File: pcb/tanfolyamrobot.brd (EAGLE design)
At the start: 81.3 x 58.7 mm, 79 parts, among them IC1 STM32F10XRXT6, IC2 7805, IC4 FT232RL, IC5 LD117AS33TR, M1 DRV8833, Q1 16MHz, Q2 BSS123, Q3 BSS123, Q4 BSS123, X2 PWR, X6 KUSBVX-BS1N

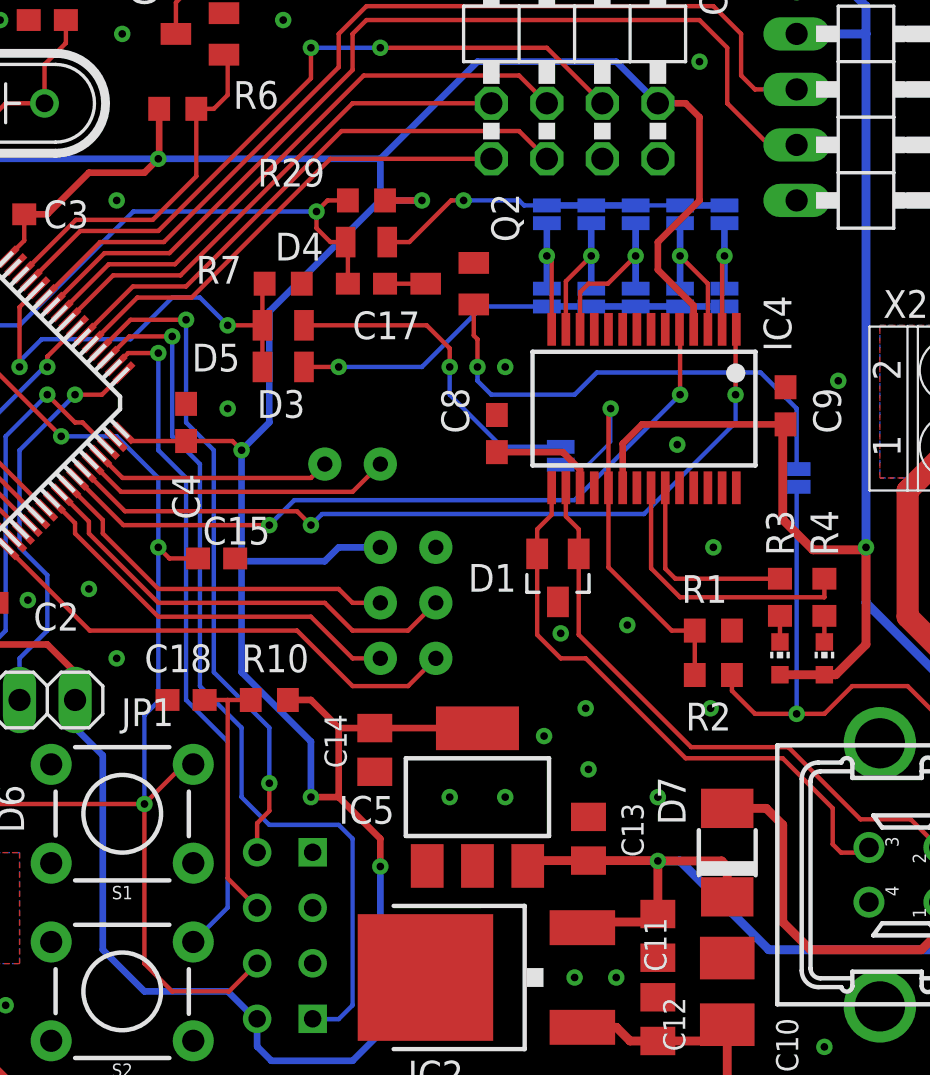
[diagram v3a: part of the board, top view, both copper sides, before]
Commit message: moved 5V_USB reset's cap to the gate of the mosfet (#1)
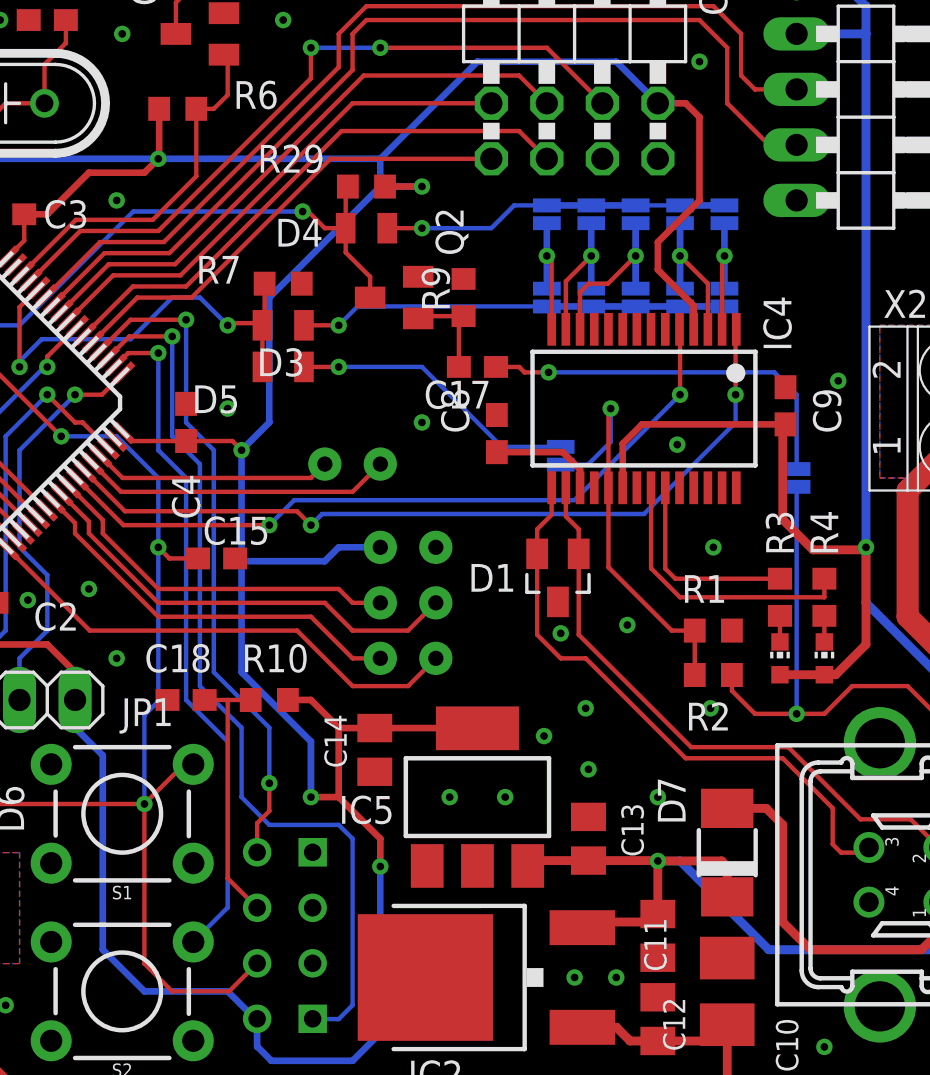
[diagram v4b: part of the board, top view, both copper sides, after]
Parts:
- added R9: 10K, rcl:R0603
- C17: value 22n -> 2u2
- moved C17 6.35 mm to (55.2, 34.9), turned to 180 degrees
- moved Q2 2.62 mm to (51.4, 38.1)
- moved D3 1.91 mm to (46.4, 36.8)
- moved D5 1.91 mm to (46.4, 34.9)
- moved D4 0.63 mm to (50.2, 41.3)
- moved R29 0.63 mm to (50.2, 43.2)
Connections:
- removed net N$6: JP14.2, Q2.1
- removed net N$9: C17.2, Q2.3
- new net N$2: C17.2, Q2.1, R9.1
- new net N$4: C17.1, JP14.2
- net GND: now also R9.2
- net RSTN: now also Q2.3; no longer C17.1
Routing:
- net N$6: track 22.3 -> 0.00 mm, vias 1 -> 0
- net N$4: track 0.00 -> 17.7 mm, vias 0 -> 1
- net N$2: track 0.00 -> 4.53 mm
- net N$8: track 15.3 -> 13.3 mm
- net N$9: track 1.86 -> 0.00 mm
- net RSTN: track 81.5 -> 83.3 mm
- net FTDI_BOOT0_OUT: track 20.4 -> 19.6 mm

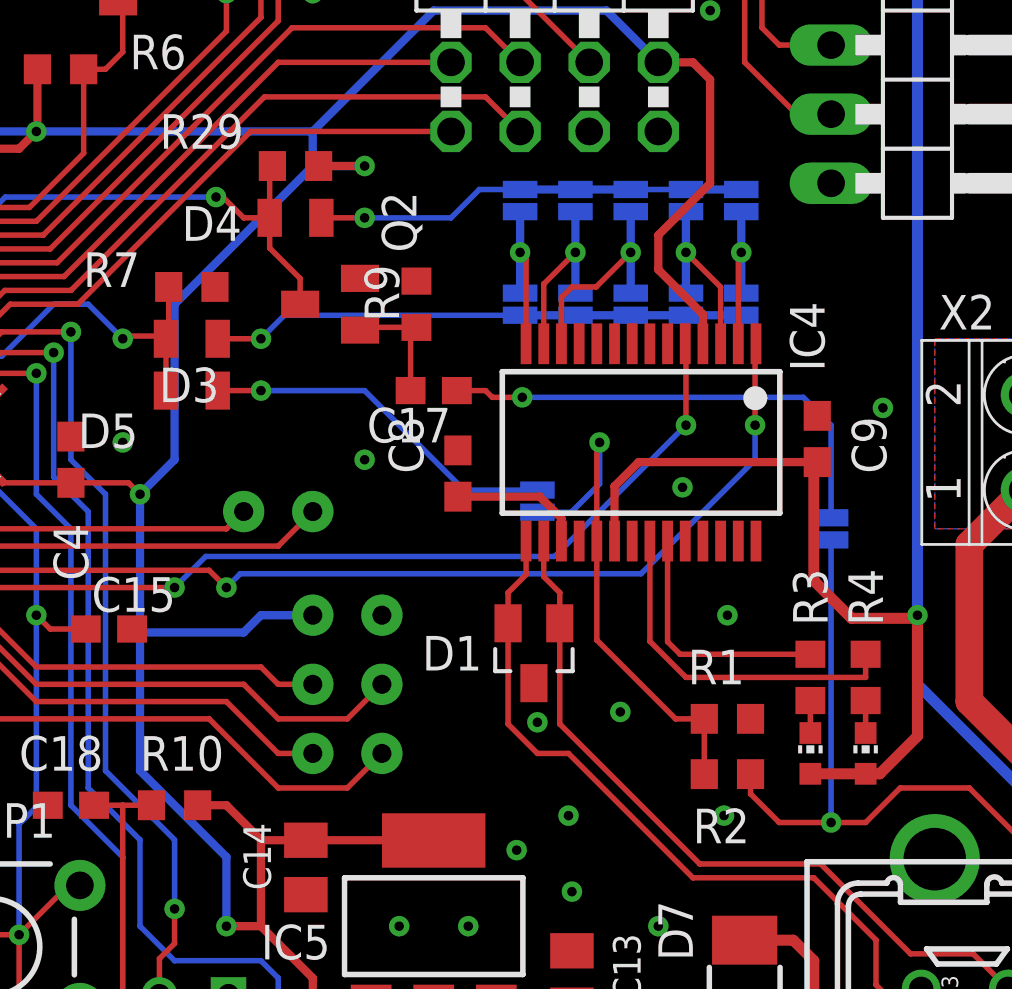
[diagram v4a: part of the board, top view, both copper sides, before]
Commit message: changed all solder jumpers to resistors (#1)
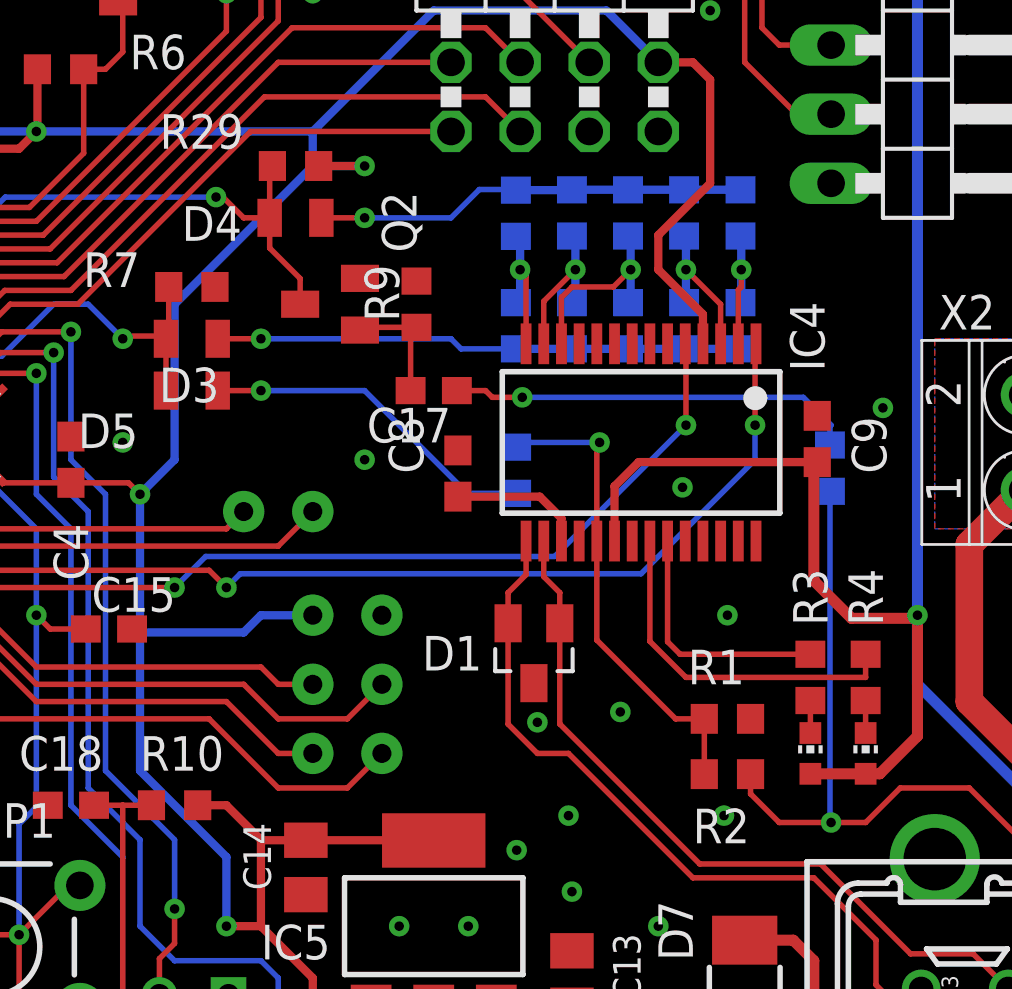
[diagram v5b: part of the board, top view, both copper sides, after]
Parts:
- removed JP10, JP11, JP12, JP13, JP14, JP15, JP2, JP3, JP4, JP5, JP8, JP9: JUMPER-SMT_2_NO_NO-SILK, SparkFun-Jumpers:SMT-JUMPER_2_NO_NO-SILK
- added R11, R12, R13, R14, R15, R16, R17, R18, R19, R26, R27, R28: 0R, rcl:R0603
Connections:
- net 5V_USB: now also R27.1; no longer JP14.1
- net FTDI_BOOT0_OUT: now also R12.2, R14.2, R16.2, R18.2, R26.2; no longer JP11.2, JP13.2, JP3.2, JP5.2, JP9.2
- net FTDI_CBUS2: now also R15.1, R16.1; no longer JP8.1, JP9.1
- net FTDI_CBUS3: now also R17.1, R18.1; no longer JP10.1, JP11.1
- net FTDI_CBUS4: now also R19.1, R26.1; no longer JP12.1, JP13.1
- net FTDI_DTRN: now also R13.1, R14.1; no longer JP4.1, JP5.1
- net FTDI_RSTN: now also R28.1; no longer JP15.1
- net FTDI_RSTN_OUT: now also R11.2, R13.2, R15.2, R17.2, R19.2; no longer JP10.2, JP12.2, JP2.2, JP4.2, JP8.2
- net FTDI_RTSN: now also R11.1, R12.1; no longer JP2.1, JP3.1
- net N$4: now also R27.2; no longer JP14.2
- net N$8: now also R28.2; no longer JP15.2
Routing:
- net N$4: track 17.7 -> 15.0 mm
- net 5V_USB: track 49.5 -> 51.3 mm
- net FTDI_DTRN: track 6.40 -> 5.24 mm
- net FTDI_RTSN: track 6.88 -> 5.76 mm
- net FTDI_RSTN: track 18.7 -> 17.6 mm
- net FTDI_CBUS2: track 6.84 -> 5.76 mm
- net FTDI_CBUS3: track 6.45 -> 5.38 mm
- net FTDI_CBUS4: track 7.93 -> 7.20 mm
- net N$8: track 13.3 -> 12.5 mm

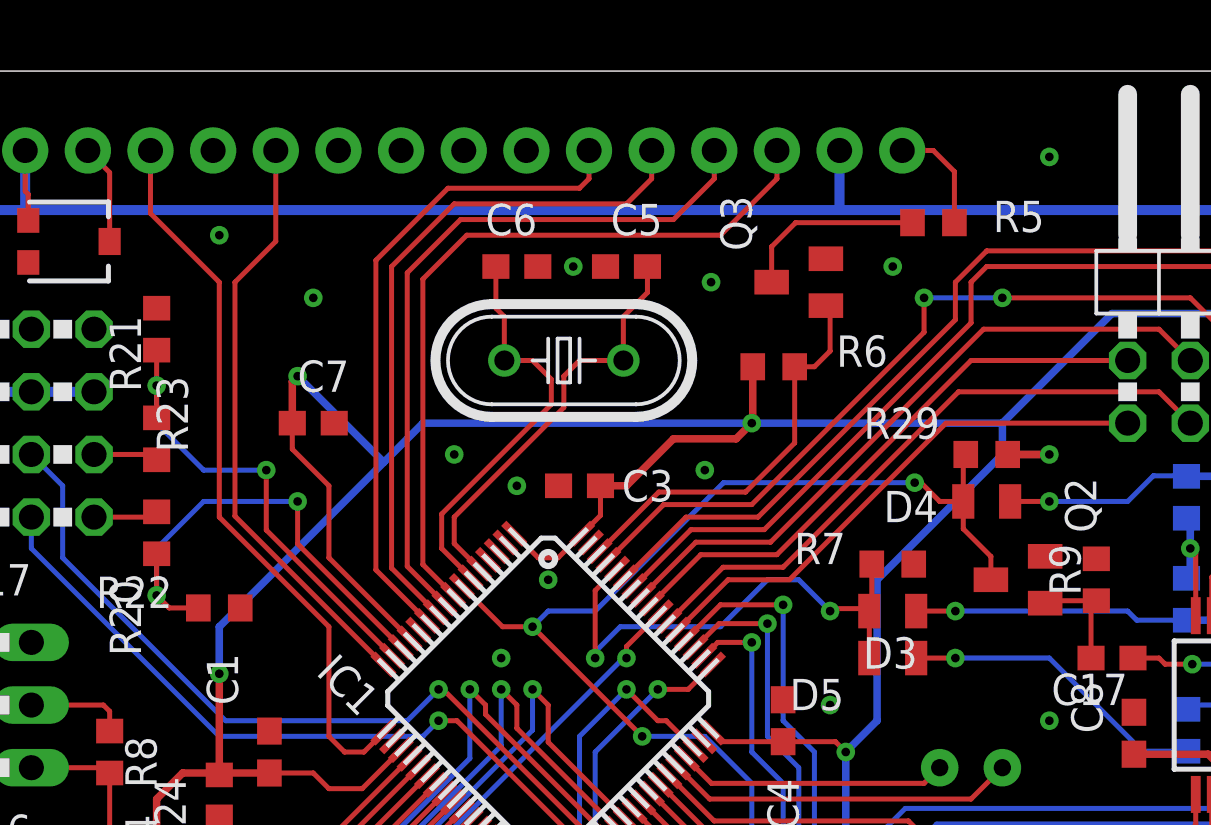
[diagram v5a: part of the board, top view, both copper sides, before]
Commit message: changed xtal to smd resonator (#1)
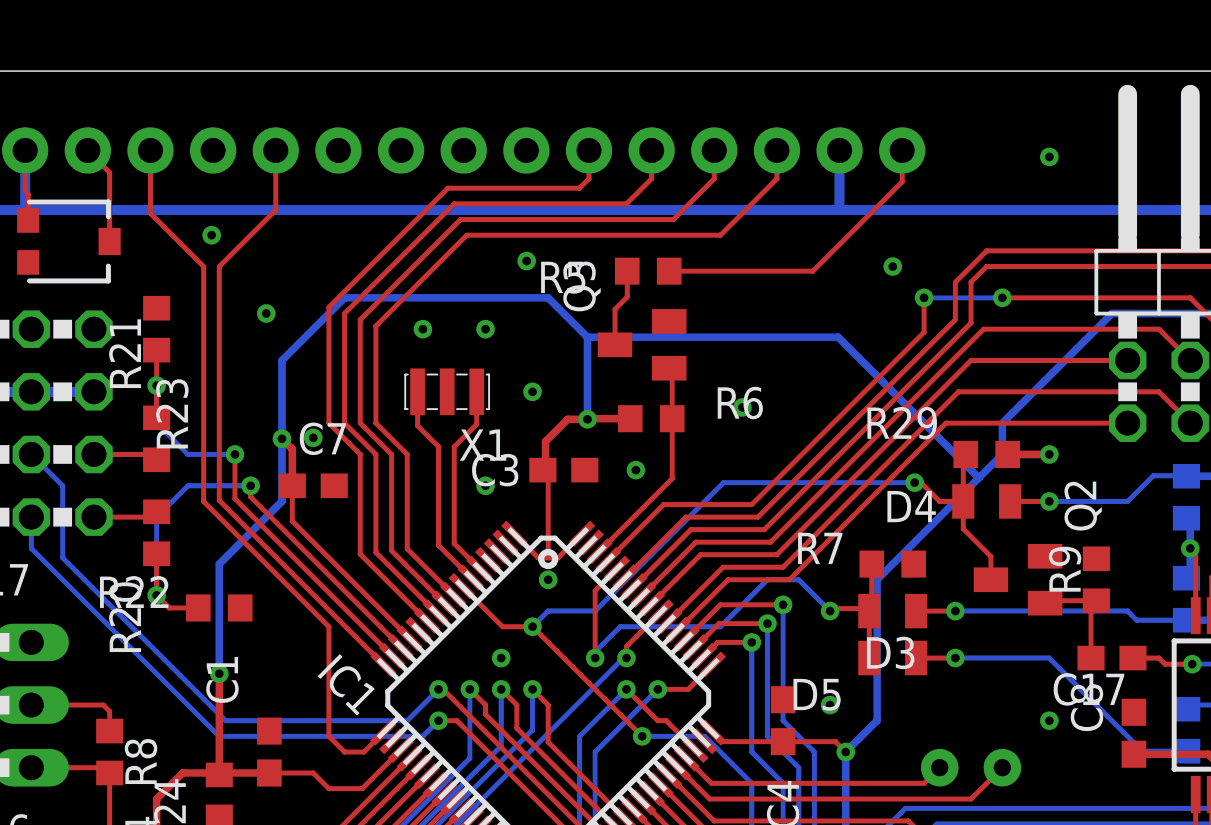
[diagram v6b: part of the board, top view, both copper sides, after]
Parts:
- removed C5, C6: 15p, rcl:C0603
- removed Q1: 16MHz, crystal:HC49U-V
- added X1: CSTCE08M, resonator:CSTCE
- moved R5 11.7 mm to (36.4, 50.6), turned to 0 degrees
- moved Q3 6.84 mm to (36.2, 47.6)
- moved R6 5.39 mm to (36.6, 44.6)
- moved C7 2.54 mm to (22.9, 41.9)
- moved C3 0.90 mm to (33.0, 42.5), turned to 0 degrees
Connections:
- removed net LCD_K: LCD1.16, R5.1
- new net N$6: LCD1.16, R5.2
- net GND: now also X1.2; no longer C5.2, C6.2
- net N$1: now also R5.1; no longer R5.2
- net OSCIN: now also X1.1; no longer C5.1, Q1.1
- net OSCOUT: now also X1.3; no longer C6.1, Q1.2
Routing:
- net N$6: track 0.00 -> 12.2 mm
- net OSCIN: track 17.0 -> 7.97 mm
- net OSCOUT: track 16.5 -> 8.41 mm
- net LCD_BACKLIGHT: track 16.4 -> 8.68 mm
- net LCD_K: track 4.54 -> 0.00 mm
- net N$1: track 7.55 -> 3.19 mm
- net +3V3: track 242.8 -> 244.8 mm
- net LCD_D7: track 30.5 -> 32.1 mm
- net LCD_D5: track 27.9 -> 29.5 mm
- net LCD_D6: track 29.2 -> 30.8 mm
- net LCD_D4: track 26.6 -> 28.2 mm
- net LCD_EN: track 24.0 -> 24.5 mm
- net ENC1_A_3V3: track 19.6 -> 20.2 mm
- net GND: vias 55 -> 58

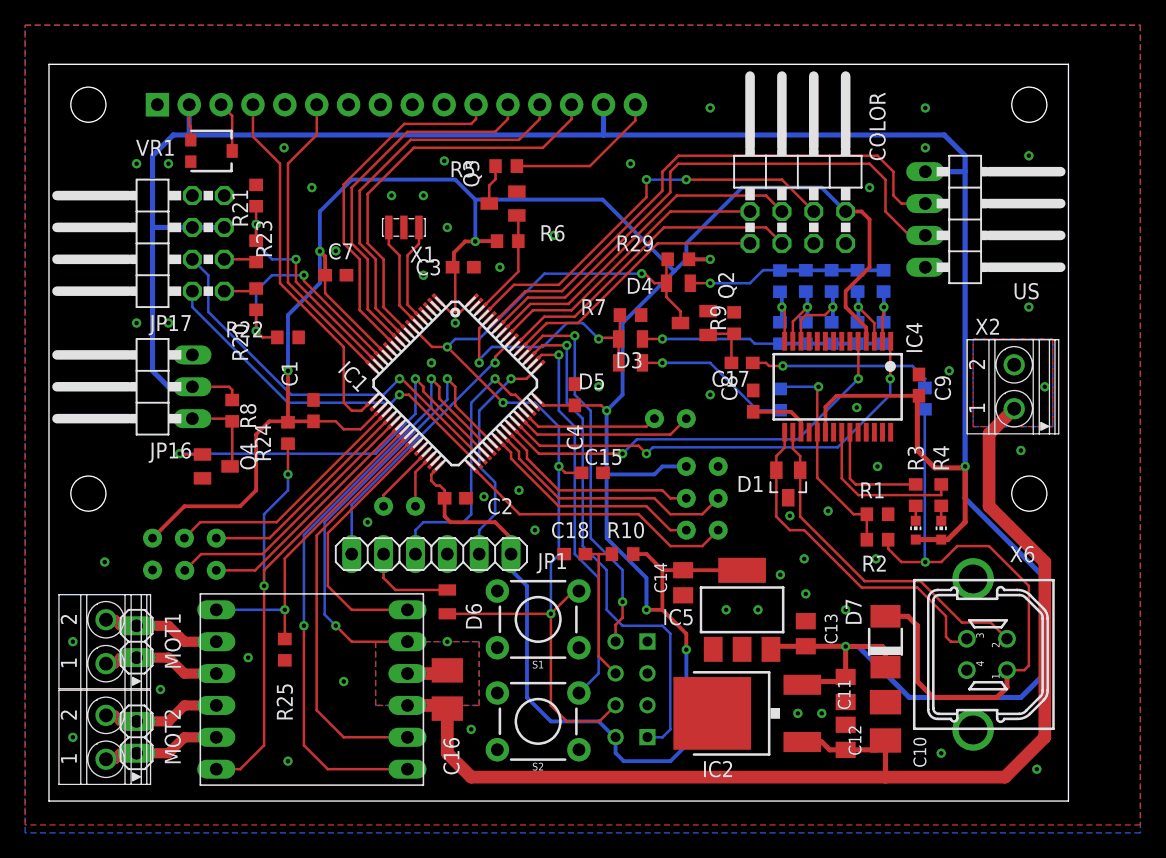
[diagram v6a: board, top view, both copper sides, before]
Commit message: changed USB transil diode packge (#1)
and also had to redesign a lot of stuff around the USB connector and FTDI chip
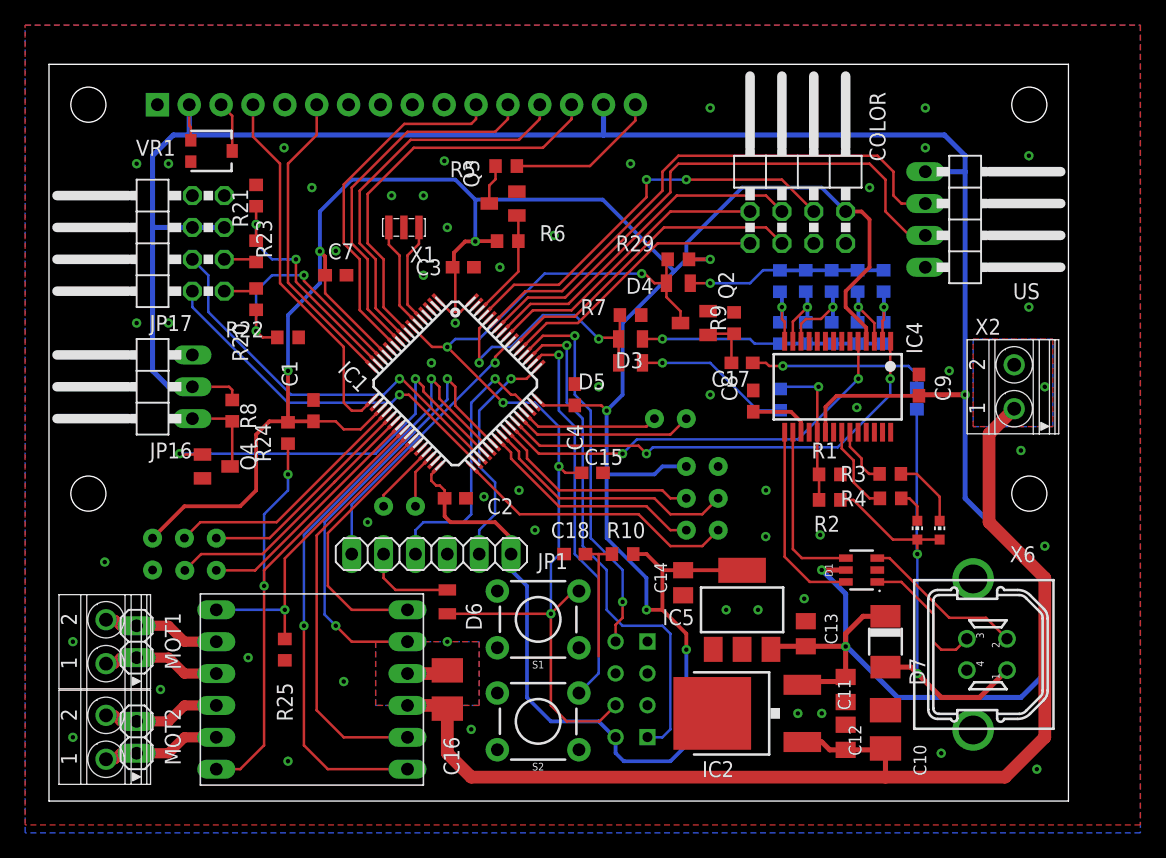
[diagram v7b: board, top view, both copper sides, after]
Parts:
- D1: value (none) -> 5Vdc; device diode:SOT23 -> Wurth_EMC Components_WE-TVS:WE-TVS_SOT23-6L
- moved D1 9.01 mm to (64.8, 18.4), turned to 90 degrees
- moved R1 4.96 mm to (62.2, 26.0)
- moved R2 4.96 mm to (62.2, 24.0)
- moved R4 4.05 mm to (67.1, 24.1), turned to 180 degrees
- moved R3 2.64 mm to (67.1, 26.1), turned to 180 degrees
- moved LED1 1.91 mm to (71.0, 21.6)
- moved LED2 1.91 mm to (69.2, 21.6)
- moved C10 0.63 mm to (66.7, 5.71)
- moved R27 0.63 mm to (69.2, 32.1)
- turned D7 to 270 degrees
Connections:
- net N$5 renamed FTDI_TXLEDN_R
- net N$7 renamed FTDI_RXLEDN_R
- removed net 5V_USB: D7.A, R2.2, R27.1, X6.1
- new net +5V/1: D7.A, LED1.A, LED2.A, R2.2, R27.1, X6.1
- new net USB_DM: D1.3, X6.2
- new net USB_DP: D1.1, X6.3
- net +5V: now also D1.5; no longer LED1.A, LED2.A
- net GND: now also D1.2; no longer D1.3
- net USB_DM_FTDI: now also D1.4; no longer D1.1, X6.2
- net USB_DP_FTDI: now also D1.6; no longer D1.2, X6.3
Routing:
- net 5V_USB: track 51.3 -> 0.00 mm, vias 1 -> 0
- net +5V/1: track 0.00 -> 43.0 mm, vias 0 -> 2
- net USB_DM_FTDI: track 27.5 -> 13.8 mm
- net USB_DM: track 0.00 -> 13.0 mm
- net USB_DP_FTDI: track 27.4 -> 15.6 mm
- net USB_DP: track 0.00 -> 11.0 mm
- net FTDI_RXLEDN: track 13.0 -> 7.01 mm
- net FTDI_RSTN: track 17.6 -> 12.3 mm
- net +5V: track 214.3 -> 209.3 mm, vias 2 -> 3
- net FTDI_TXLEDN_R: track 1.19 -> 5.76 mm
- net FTDI_TXLEDN: track 9.14 -> 4.79 mm
- net N$3: track 12.2 -> 10.3 mm
- net FTDI_RXLEDN_R: track 1.19 -> 2.70 mm
- net VCC: track 95.5 -> 94.6 mm
- net BOOT0: track 21.1 -> 21.6 mm
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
